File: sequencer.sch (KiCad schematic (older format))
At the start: 27 parts, among them U101 74HCT125, U102 74HC595, U103 74HC595, U104 74HC595, U105 74HC165

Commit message: last minute fixes
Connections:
- net GND: now also U105.10 (SER)
- net SR_MISO: now also U105.9 (QH); no longer U105.10 (SER)
- no-connect marks 5 -> 4
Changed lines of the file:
@@
 Text GLabel 7200 5500 2    51   Input ~ 0
 SCOL4
-Text GLabel 5100 5600 0    51   Output ~ 0
+Text GLabel 5100 5500 0    51   Output ~ 0
 SR_MISO
 Text GLabel 8900 1700 0    51   BiDi ~ 0
@@
 	5100 5300 5500 5300
 Wire Wire Line
-	5100 5600 5500 5600
+	5100 5500 5500 5500
 Wire Wire Line
 	6500 5100 7200 5100
@@
 NoConn ~ 9200 1100
 Wire Wire Line
-	5400 5700 5400 5900
+	5400 5600 5400 5900
 Connection ~ 5400 5800
-NoConn ~ 5500 5500
 NoConn ~ 5500 4300
+Wire Wire Line
+	5500 5600 5400 5600
+Connection ~ 5400 5700
 $EndSCHEMATC

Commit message: work in progress
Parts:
- added Q101: MMBT3904, TO_SOT_Packages_SMD:SOT-23, symbol MMBT3904
- added R114, R115, R116, R117: 33k, Resistors_SMD:R_0603_HandSoldering, symbol R
- added R118: 1k, Resistors_SMD:R_0603_HandSoldering, symbol R
- added R119: 1M, Resistors_SMD:R_0603_HandSoldering, symbol R
- added R120, R122: 10k, Resistors_SMD:R_0603_HandSoldering, symbol R
- added R121: 100k, Resistors_SMD:R_0603_HandSoldering, symbol R
- C101, C102, C103, C104, C105: footprint Capacitors_SMD:C_0603 -> Capacitors_SMD:C_0603_HandSoldering
- R101, R102, R103, R104, R105, R106, R107, R108, R109, R110, R111, R112, R113: footprint Resistors_SMD:R_0603 -> Resistors_SMD:R_0603_HandSoldering
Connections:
- net +3V3: now also R114.2, R115.2, R116.2, R117.2
- net +5V: now also R118.1
- net GND: now also Q101.2 (E), R119.1, R121.2, R122.2; no longer JP103.3 (CMD), U102.13 (~OE~), U103.13 (~OE~), U104.13 (~OE~)
- net LCD_RES: now also R122.1
- net SDIO_CMD: now also JP103.3 (CMD), R116.1; no longer JP103.2 (DAT3/CD)
- net SDIO_D0: now also R115.1
- net at JP103.1 (DAT2): now also R117.1
- net at JP103.8 (DAT1): now also R114.1
- new net: Q101.3 (C), R118.2, U102.13 (~OE~), U103.13 (~OE~), U104.13 (~OE~)
- new net: Q101.1 (B), R120.1, R121.1
- new net SDIO_CD: JP103.2 (DAT3/CD), R119.2
- new net SR_OE: R120.2
- no-connect marks 4 -> 2
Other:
- note added: "NEW"
- moved on the sheet: ENC101, JP102, JP103

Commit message: work in progress
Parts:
- C101, C102, C103, C104, C105: footprint Capacitors_SMD:C_0603_HandSoldering -> w_capacitor:C_0603
- R101, R102, R103, R104, R105, R106, R107, R108, R109, R110, R111, R112, R113, R114, R115, R116, R117, R118, R119, R120, R121, R122: footprint Resistors_SMD:R_0603_HandSoldering -> w_resistor:R_0603
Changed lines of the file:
@@
 F 0 "C101" H 5025 6950 50  0000 L CNN
 F 1 "100n" H 5025 6750 50  0000 L CNN
-F 2 "Capacitors_SMD:C_0603_HandSoldering" H 5038 6700 50  0001 C CNN
+F 2 "w_capacitor:C_0603" H 5038 6700 50  0001 C CNN
 F 3 "http://datasheet.octopart.com/GRM188R71E104JA01J-Murata-datasheet-66077098.pdf" H 5000 6850 50  0001 C CNN
 F 4 "Murata" H 5025 7050 50  0001 C CNN "MFN"
@@
 F 0 "C102" H 5325 6950 50  0000 L CNN
 F 1 "100n" H 5325 6750 50  0000 L CNN
-F 2 "Capacitors_SMD:C_0603_HandSoldering" H 5338 6700 50  0001 C CNN
+F 2 "w_capacitor:C_0603" H 5338 6700 50  0001 C CNN
 F 3 "http://datasheet.octopart.com/GRM188R71E104JA01J-Murata-datasheet-66077098.pdf" H 5300 6850 50  0001 C CNN
 F 4 "Murata" H 5325 7050 50  0001 C CNN "MFN"
@@
 F 0 "C103" H 5625 6950 50  0000 L CNN
 F 1 "100n" H 5625 6750 50  0000 L CNN
-F 2 "Capacitors_SMD:C_0603_HandSoldering" H 5638 6700 50  0001 C CNN
+F 2 "w_capacitor:C_0603" H 5638 6700 50  0001 C CNN
 F 3 "http://datasheet.octopart.com/GRM188R71E104JA01J-Murata-datasheet-66077098.pdf" H 5600 6850 50  0001 C CNN
 F 4 "Murata" H 5625 7050 50  0001 C CNN "MFN"
@@
 F 0 "C104" H 5925 6950 50  0000 L CNN
 F 1 "100n" H 5925 6750 50  0000 L CNN
-F 2 "Capacitors_SMD:C_0603_HandSoldering" H 5938 6700 50  0001 C CNN
+F 2 "w_capacitor:C_0603" H 5938 6700 50  0001 C CNN
 F 3 "http://datasheet.octopart.com/GRM188R71E104JA01J-Murata-datasheet-66077098.pdf" H 5900 6850 50  0001 C CNN
 F 4 "Murata" H 5925 7050 50  0001 C CNN "MFN"
@@
 F 0 "C105" H 6225 6950 50  0000 L CNN
 F 1 "100n" H 6225 6750 50  0000 L CNN
-F 2 "Capacitors_SMD:C_0603_HandSoldering" H 6238 6700 50  0001 C CNN
+F 2 "w_capacitor:C_0603" H 6238 6700 50  0001 C CNN
 F 3 "http://datasheet.octopart.com/GRM188R71E104JA01J-Murata-datasheet-66077098.pdf" H 6200 6850 50  0001 C CNN
 F 4 "Murata" H 6225 7050 50  0001 C CNN "MFN"
@@
 F 0 "R101" V 6650 5100 50  0000 L CNN
 F 1 "10k" V 6700 4950 50  0000 C CNN
-F 2 "Resistors_SMD:R_0603_HandSoldering" V 6630 4950 50  0001 C CNN
+F 2 "w_resistor:R_0603" V 6630 4950 50  0001 C CNN
 F 3 "http://datasheet.octopart.com/ERJ-3EKF1002V-Panasonic-datasheet-13266541.pdf" H 6700 4950 50  0001 C CNN
 F 4 "Panasonic" H 6650 5200 50  0001 C CNN "MFN"
@@
 F 0 "R102" V 6750 5100 50  0000 L CNN
 F 1 "10k" V 6800 4950 50  0000 C CNN
-F 2 "Resistors_SMD:R_0603_HandSoldering" V 6730 4950 50  0001 C CNN
+F 2 "w_resistor:R_0603" V 6730 4950 50  0001 C CNN
 F 3 "http://datasheet.octopart.com/ERJ-3EKF1002V-Panasonic-datasheet-13266541.pdf" H 6800 4950 50  0001 C CNN
 F 4 "Panasonic" H 6750 5200 50  0001 C CNN "MFN"
@@
 F 0 "R103" V 6850 5100 50  0000 L CNN
 F 1 "10k" V 6900 4950 50  0000 C CNN
-F 2 "Resistors_SMD:R_0603_HandSoldering" V 6830 4950 50  0001 C CNN
+F 2 "w_resistor:R_0603" V 6830 4950 50  0001 C CNN
 F 3 "http://datasheet.octopart.com/ERJ-3EKF1002V-Panasonic-datasheet-13266541.pdf" H 6900 4950 50  0001 C CNN
 F 4 "Panasonic" H 6850 5200 50  0001 C CNN "MFN"
@@
 F 0 "R104" V 6950 5100 50  0000 L CNN
 F 1 "10k" V 7000 4950 50  0000 C CNN
-F 2 "Resistors_SMD:R_0603_HandSoldering" V 6930 4950 50  0001 C CNN
+F 2 "w_resistor:R_0603" V 6930 4950 50  0001 C CNN
 F 3 "http://datasheet.octopart.com/ERJ-3EKF1002V-Panasonic-datasheet-13266541.pdf" H 7000 4950 50  0001 C CNN
 F 4 "Panasonic" H 6950 5200 50  0001 C CNN "MFN"
@@
 F 0 "R105" V 7050 5100 50  0000 L CNN
 F 1 "10k" V 7100 4950 50  0000 C CNN
-F 2 "Resistors_SMD:R_0603_HandSoldering" V 7030 4950 50  0001 C CNN
+F 2 "w_resistor:R_0603" V 7030 4950 50  0001 C CNN
 F 3 "http://datasheet.octopart.com/ERJ-3EKF1002V-Panasonic-datasheet-13266541.pdf" H 7100 4950 50  0001 C CNN
 F 4 "Panasonic" H 7050 5200 50  0001 C CNN "MFN"
@@
 F 0 "R107" V 6700 2550 50  0000 L CNN
 F 1 "470" V 6750 2400 50  0000 C CNN
-F 2 "Resistors_SMD:R_0603_HandSoldering" V 6680 2400 50  0001 C CNN
+F 2 "w_resistor:R_0603" V 6680 2400 50  0001 C CNN
 F 3 "http://datasheet.octopart.com/ERJ3EKF4700V-Panasonic-datasheet-13266541.pdf" H 6750 2400 50  0001 C CNN
 F 4 "Panasonic" H 6700 2650 50  0001 C CNN "MFN"
@@
 F 0 "R106" V 6700 2450 50  0000 L CNN
 F 1 "470" V 6750 2300 50  0000 C CNN
-F 2 "Resistors_SMD:R_0603_HandSoldering" V 6680 2300 50  0001 C CNN
+F 2 "w_resistor:R_0603" V 6680 2300 50  0001 C CNN
 F 3 "http://datasheet.octopart.com/ERJ3EKF4700V-Panasonic-datasheet-13266541.pdf" H 6750 2300 50  0001 C CNN
 F 4 "Panasonic" H 6700 2550 50  0001 C CNN "MFN"
@@
 F 0 "R108" V 6700 2650 50  0000 L CNN
 F 1 "470" V 6750 2500 50  0000 C CNN
-F 2 "Resistors_SMD:R_0603_HandSoldering" V 6680 2500 50  0001 C CNN
+F 2 "w_resistor:R_0603" V 6680 2500 50  0001 C CNN
 F 3 "http://datasheet.octopart.com/ERJ3EKF4700V-Panasonic-datasheet-13266541.pdf" H 6750 2500 50  0001 C CNN
 F 4 "Panasonic" H 6700 2750 50  0001 C CNN "MFN"
@@
 F 0 "R109" V 6700 2750 50  0000 L CNN
 F 1 "470" V 6750 2600 50  0000 C CNN
-F 2 "Resistors_SMD:R_0603_HandSoldering" V 6680 2600 50  0001 C CNN
+F 2 "w_resistor:R_0603" V 6680 2600 50  0001 C CNN
 F 3 "http://datasheet.octopart.com/ERJ3EKF4700V-Panasonic-datasheet-13266541.pdf" H 6750 2600 50  0001 C CNN
 F 4 "Panasonic" H 6700 2850 50  0001 C CNN "MFN"
@@
 F 0 "R113" V 6700 3150 50  0000 L CNN
 F 1 "470" V 6750 3000 50  0000 C CNN
-F 2 "Resistors_SMD:R_0603_HandSoldering" V 6680 3000 50  0001 C CNN
+F 2 "w_resistor:R_0603" V 6680 3000 50  0001 C CNN
 F 3 "http://datasheet.octopart.com/ERJ3EKF4700V-Panasonic-datasheet-13266541.pdf" H 6750 3000 50  0001 C CNN
 F 4 "Panasonic" H 6700 3250 50  0001 C CNN "MFN"
@@
 F 0 "R112" V 6700 3050 50  0000 L CNN
 F 1 "470" V 6750 2900 50  0000 C CNN
-F 2 "Resistors_SMD:R_0603_HandSoldering" V 6680 2900 50  0001 C CNN
+F 2 "w_resistor:R_0603" V 6680 2900 50  0001 C CNN
 F 3 "http://datasheet.octopart.com/ERJ3EKF4700V-Panasonic-datasheet-13266541.pdf" H 6750 2900 50  0001 C CNN
 F 4 "Panasonic" H 6700 3150 50  0001 C CNN "MFN"
@@
 F 0 "R111" V 6700 2950 50  0000 L CNN
 F 1 "470" V 6750 2800 50  0000 C CNN
-F 2 "Resistors_SMD:R_0603_HandSoldering" V 6680 2800 50  0001 C CNN
+F 2 "w_resistor:R_0603" V 6680 2800 50  0001 C CNN
 F 3 "http://datasheet.octopart.com/ERJ3EKF4700V-Panasonic-datasheet-13266541.pdf" H 6750 2800 50  0001 C CNN
 F 4 "Panasonic" H 6700 3050 50  0001 C CNN "MFN"
@@
 F 0 "R110" V 6700 2850 50  0000 L CNN
 F 1 "470" V 6750 2700 50  0000 C CNN
-F 2 "Resistors_SMD:R_0603_HandSoldering" V 6680 2700 50  0001 C CNN
+F 2 "w_resistor:R_0603" V 6680 2700 50  0001 C CNN
 F 3 "http://datasheet.octopart.com/ERJ3EKF4700V-Panasonic-datasheet-13266541.pdf" H 6750 2700 50  0001 C CNN
 F 4 "Panasonic" H 6700 2950 50  0001 C CNN "MFN"
@@
 F 0 "R117" V 8980 1050 50  0000 C CNN
 F 1 "33k" V 8900 1050 50  0000 C CNN
-F 2 "Resistors_SMD:R_0603_HandSoldering" V 8830 1050 50  0001 C CNN
+F 2 "w_resistor:R_0603" V 8830 1050 50  0001 C CNN
 F 3 "" H 8900 1050 50  0001 C CNN
 	1    8900 1050
@@
 F 0 "R119" V 8980 2250 50  0000 C CNN
 F 1 "1M" V 8900 2250 50  0000 C CNN
-F 2 "Resistors_SMD:R_0603_HandSoldering" V 8830 2250 50  0001 C CNN
+F 2 "w_resistor:R_0603" V 8830 2250 50  0001 C CNN
 F 3 "" H 8900 2250 50  0001 C CNN
 	1    8900 2250
@@
 F 0 "R114" V 8380 1050 50  0000 C CNN
 F 1 "33k" V 8300 1050 50  0000 C CNN
-F 2 "Resistors_SMD:R_0603_HandSoldering" V 8230 1050 50  0001 C CNN
+F 2 "w_resistor:R_0603" V 8230 1050 50  0001 C CNN
 F 3 "" H 8300 1050 50  0001 C CNN
 	1    8300 1050
@@
 F 0 "R115" V 8580 1050 50  0000 C CNN
 F 1 "33k" V 8500 1050 50  0000 C CNN
-F 2 "Resistors_SMD:R_0603_HandSoldering" V 8430 1050 50  0001 C CNN
+F 2 "w_resistor:R_0603" V 8430 1050 50  0001 C CNN
 F 3 "" H 8500 1050 50  0001 C CNN
 	1    8500 1050
@@
 F 0 "R116" V 8780 1050 50  0000 C CNN
 F 1 "33k" V 8700 1050 50  0000 C CNN
-F 2 "Resistors_SMD:R_0603_HandSoldering" V 8630 1050 50  0001 C CNN
+F 2 "w_resistor:R_0603" V 8630 1050 50  0001 C CNN
 F 3 "" H 8700 1050 50  0001 C CNN
 	1    8700 1050
@@
 F 0 "R122" V 2780 5650 50  0000 C CNN
 F 1 "10k" V 2700 5650 50  0000 C CNN
-F 2 "Resistors_SMD:R_0603_HandSoldering" V 2630 5650 50  0001 C CNN
+F 2 "w_resistor:R_0603" V 2630 5650 50  0001 C CNN
 F 3 "" H 2700 5650 50  0001 C CNN
 	1    2700 5650
@@
 F 0 "R118" V 4180 2150 50  0000 C CNN
 F 1 "1k" V 4100 2150 50  0000 C CNN
-F 2 "Resistors_SMD:R_0603_HandSoldering" V 4030 2150 50  0001 C CNN
+F 2 "w_resistor:R_0603" V 4030 2150 50  0001 C CNN
 F 3 "http://datasheet.octopart.com/ERJ-3EKF1001V-Panasonic-datasheet-82288794.pdf" H 4100 2150 50  0001 C CNN
 F 4 "Panasonic" H 4180 2250 50  0001 C CNN "MFN"
@@
 F 0 "R120" V 3530 2700 50  0000 C CNN
 F 1 "10k" V 3450 2700 50  0000 C CNN
-F 2 "Resistors_SMD:R_0603_HandSoldering" V 3380 2700 50  0001 C CNN
+F 2 "w_resistor:R_0603" V 3380 2700 50  0001 C CNN
 F 3 "" H 3450 2700 50  0001 C CNN
 	1    3450 2700
@@
 F 0 "R121" V 3780 2950 50  0000 C CNN
 F 1 "100k" V 3700 2950 50  0000 C CNN
-F 2 "Resistors_SMD:R_0603_HandSoldering" V 3630 2950 50  0001 C CNN
+F 2 "w_resistor:R_0603" V 3630 2950 50  0001 C CNN
 F 3 "" H 3700 2950 50  0001 C CNN
 	1    3700 2950

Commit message: cleanup
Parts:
- R114, R115, R116, R117: MFN (none) -> Panasonic; MFP (none) -> ERJ-3EKF3302V
- R119: MFN (none) -> Panasonic; MFP (none) -> ERJ-3EKF1004V
- R120, R122: MFN (none) -> Panasonic; MFP (none) -> ERJ-3EKF1002V
- R121: MFN (none) -> Panasonic; MFP (none) -> ERJ-3EKF1003V
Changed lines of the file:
@@
 F 1 "33k" V 8900 1050 50  0000 C CNN
 F 2 "w_resistor:R_0603" V 8830 1050 50  0001 C CNN
-F 3 "" H 8900 1050 50  0001 C CNN
+F 3 "http://datasheet.octopart.com/ERJ3EKF3302V-Panasonic-datasheet-13266541.pdf" H 8900 1050 50  0001 C CNN
+F 4 "Panasonic" H 8980 1150 50  0001 C CNN "MFN"
+F 5 "ERJ-3EKF3302V" H 8980 1150 50  0001 C CNN "MFP"
 	1    8900 1050
 	-1   0    0    1
@@
 F 1 "1M" V 8900 2250 50  0000 C CNN
 F 2 "w_resistor:R_0603" V 8830 2250 50  0001 C CNN
-F 3 "" H 8900 2250 50  0001 C CNN
+F 3 "http://datasheet.octopart.com/ERJ-3EKF1004V-Panasonic-datasheet-13266541.pdf" H 8900 2250 50  0001 C CNN
+F 4 "Panasonic" H 8980 2350 50  0001 C CNN "MFN"
+F 5 "ERJ-3EKF1004V" H 8980 2350 50  0001 C CNN "MFP"
 	1    8900 2250
 	-1   0    0    1
@@
 F 1 "33k" V 8300 1050 50  0000 C CNN
 F 2 "w_resistor:R_0603" V 8230 1050 50  0001 C CNN
-F 3 "" H 8300 1050 50  0001 C CNN
+F 3 "http://datasheet.octopart.com/ERJ3EKF3302V-Panasonic-datasheet-13266541.pdf" H 8300 1050 50  0001 C CNN
+F 4 "Panasonic" H 8380 1150 50  0001 C CNN "MFN"
+F 5 "ERJ-3EKF3302V" H 8380 1150 50  0001 C CNN "MFP"
 	1    8300 1050
 	-1   0    0    1
@@
 F 1 "33k" V 8500 1050 50  0000 C CNN
 F 2 "w_resistor:R_0603" V 8430 1050 50  0001 C CNN
-F 3 "" H 8500 1050 50  0001 C CNN
+F 3 "http://datasheet.octopart.com/ERJ3EKF3302V-Panasonic-datasheet-13266541.pdf" H 8500 1050 50  0001 C CNN
+F 4 "Panasonic" H 8580 1150 50  0001 C CNN "MFN"
+F 5 "ERJ-3EKF3302V" H 8580 1150 50  0001 C CNN "MFP"
 	1    8500 1050
 	-1   0    0    1
@@
 F 1 "33k" V 8700 1050 50  0000 C CNN
 F 2 "w_resistor:R_0603" V 8630 1050 50  0001 C CNN
-F 3 "" H 8700 1050 50  0001 C CNN
+F 3 "http://datasheet.octopart.com/ERJ3EKF3302V-Panasonic-datasheet-13266541.pdf" H 8700 1050 50  0001 C CNN
+F 4 "Panasonic" H 8780 1150 50  0001 C CNN "MFN"
+F 5 "ERJ-3EKF3302V" H 8780 1150 50  0001 C CNN "MFP"
 	1    8700 1050
 	-1   0    0    1
@@
 F 1 "10k" V 2700 5650 50  0000 C CNN
 F 2 "w_resistor:R_0603" V 2630 5650 50  0001 C CNN
-F 3 "" H 2700 5650 50  0001 C CNN
+F 3 "http://datasheet.octopart.com/ERJ-3EKF1002V-Panasonic-datasheet-13266541.pdf" H 2700 5650 50  0001 C CNN
+F 4 "Panasonic" H 2780 5750 50  0001 C CNN "MFN"
+F 5 "ERJ-3EKF1002V" H 2780 5750 50  0001 C CNN "MFP"
 	1    2700 5650
 	1    0    0    -1
@@
 F 1 "10k" V 3450 2700 50  0000 C CNN
 F 2 "w_resistor:R_0603" V 3380 2700 50  0001 C CNN
-F 3 "" H 3450 2700 50  0001 C CNN
+F 3 "http://datasheet.octopart.com/ERJ-3EKF1002V-Panasonic-datasheet-13266541.pdf" H 3450 2700 50  0001 C CNN
+F 4 "Panasonic" H 3530 2800 50  0001 C CNN "MFN"
+F 5 "ERJ-3EKF1002V" H 3530 2800 50  0001 C CNN "MFP"
 	1    3450 2700
 	0    1    1    0
@@
 F 1 "100k" V 3700 2950 50  0000 C CNN
 F 2 "w_resistor:R_0603" V 3630 2950 50  0001 C CNN
-F 3 "" H 3700 2950 50  0001 C CNN
+F 3 "http://datasheet.octopart.com/ERJ-3EKF1003V-Panasonic-datasheet-82288794.pdf" H 3700 2950 50  0001 C CNN
+F 4 "Panasonic" H 3780 3050 50  0001 C CNN "MFN"
+F 5 "ERJ-3EKF1003V" H 3780 3050 50  0001 C CNN "MFP"
 	1    3700 2950
 	1    0    0    -1

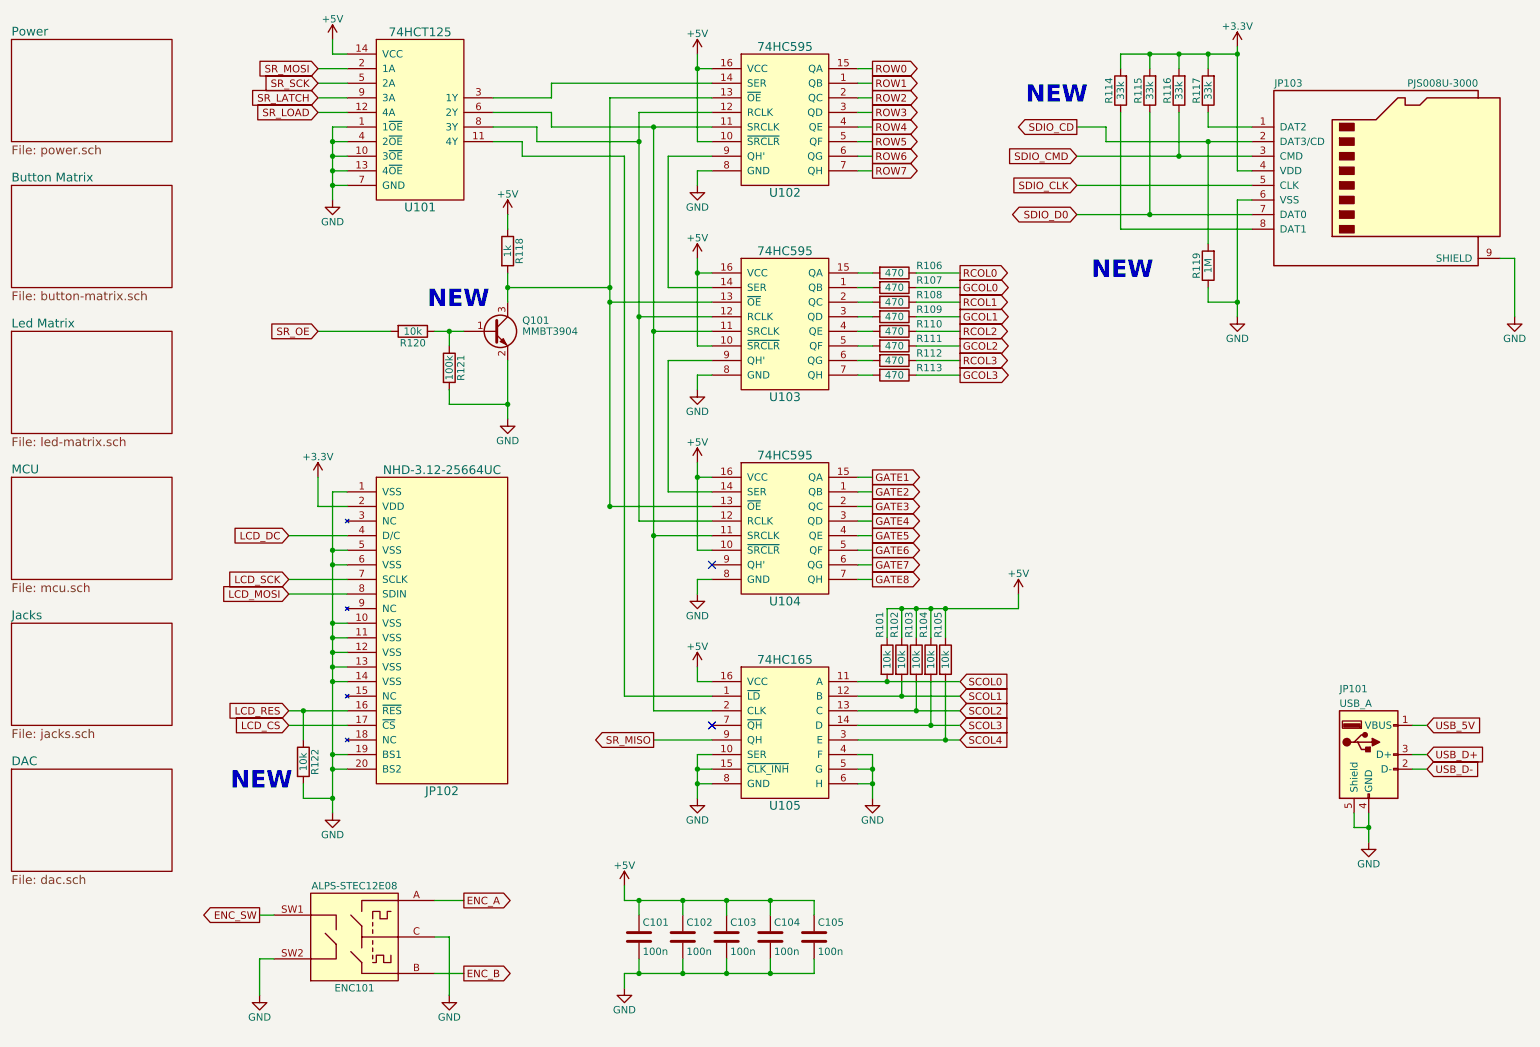
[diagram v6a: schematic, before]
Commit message: added Global schematic and only leave sheets in root schematic
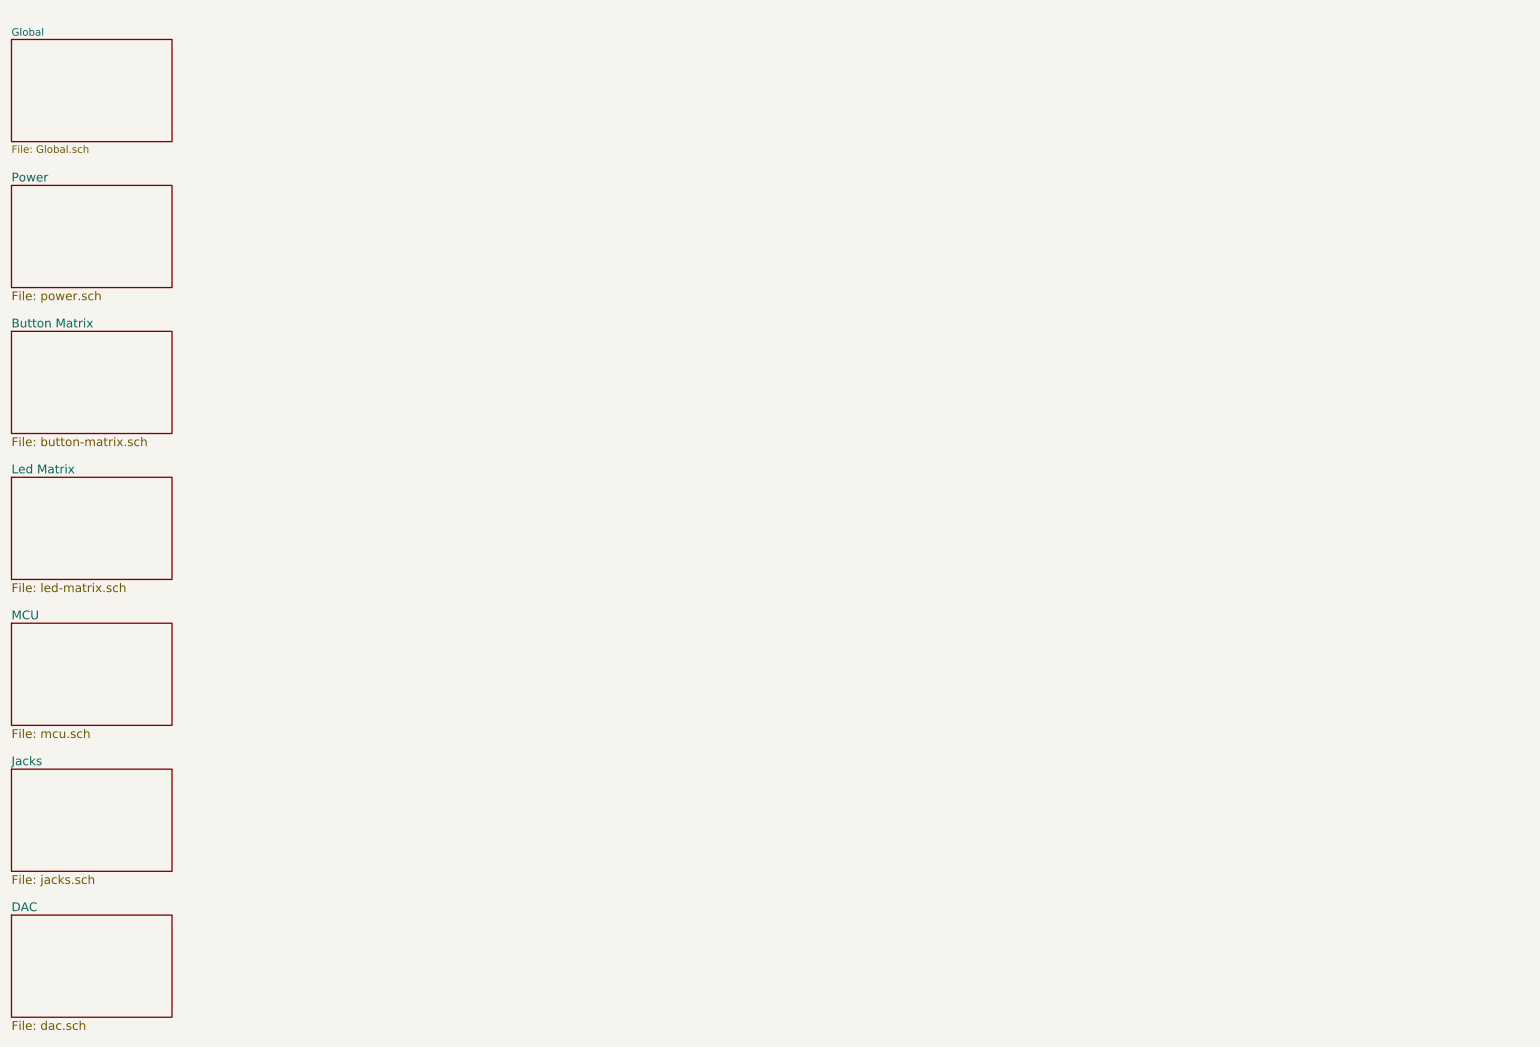
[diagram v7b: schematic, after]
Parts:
- removed C101, C102, C103, C104, C105: 100n, w_capacitor:C_0603, symbol C
- removed ENC101: ALPS-STEC12E08, w_rotary_encoder:ALPS_STEC12E08, symbol ALPS-STEC12E08
- removed JP101: USB_A, w_connector:MOLEX_USB_105057, symbol USB_A
- removed JP102: NHD-3.12-25664UC, w_lcd:NHD-3.12-25664UC, symbol NHD-3.12-25664UC
- removed JP103: PJS008U-3000, w_connector:PJS008U-3000-0, symbol Micro_SD_Card
- removed Q101: MMBT3904, TO_SOT_Packages_SMD:SOT-23, symbol MMBT3904
- removed R101, R102, R103, R104, R105, R120, R122: 10k, w_resistor:R_0603, symbol R
- removed R106, R107, R108, R109, R110, R111, R112, R113: 470, w_resistor:R_0603, symbol R
- removed R114, R115, R116, R117: 33k, w_resistor:R_0603, symbol R
- removed R118: 1k, w_resistor:R_0603, symbol R
- removed R119: 1M, w_resistor:R_0603, symbol R
- removed R121: 100k, w_resistor:R_0603, symbol R
- removed U101: 74HCT125, Housings_SOIC:SOIC-14_3.9x8.7mm_Pitch1.27mm, symbol 74HCT125
- removed U102, U103, U104: 74HC595, Housings_SOIC:SOIC-16_3.9x9.9mm_Pitch1.27mm, symbol 74HC595
- removed U105: 74HC165, Housings_SOIC:SOIC-16_3.9x9.9mm_Pitch1.27mm, symbol 74HC165
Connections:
- no-connect marks 2 -> 0
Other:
- note removed: "NEW"
